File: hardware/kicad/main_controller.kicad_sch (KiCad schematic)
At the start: 39 parts, among them J3 Tag-Connect_TC2050-IDC-NL, SW1 KMR233GLFG, SW2 KMR233GLFG, U6 ESP32-S3-MINI-1, Y1 32.768 kHz

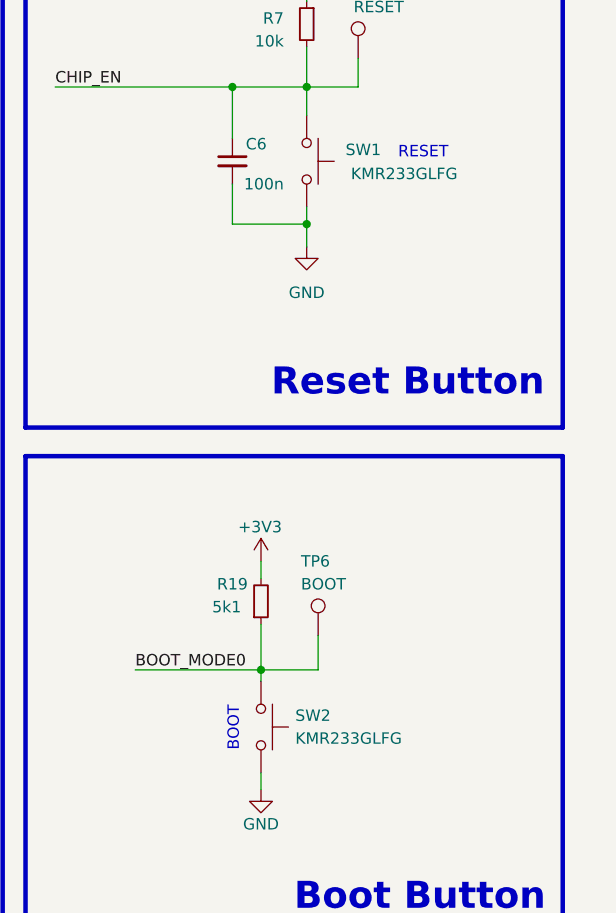
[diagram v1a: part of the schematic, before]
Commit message: fix incorrect bill of material
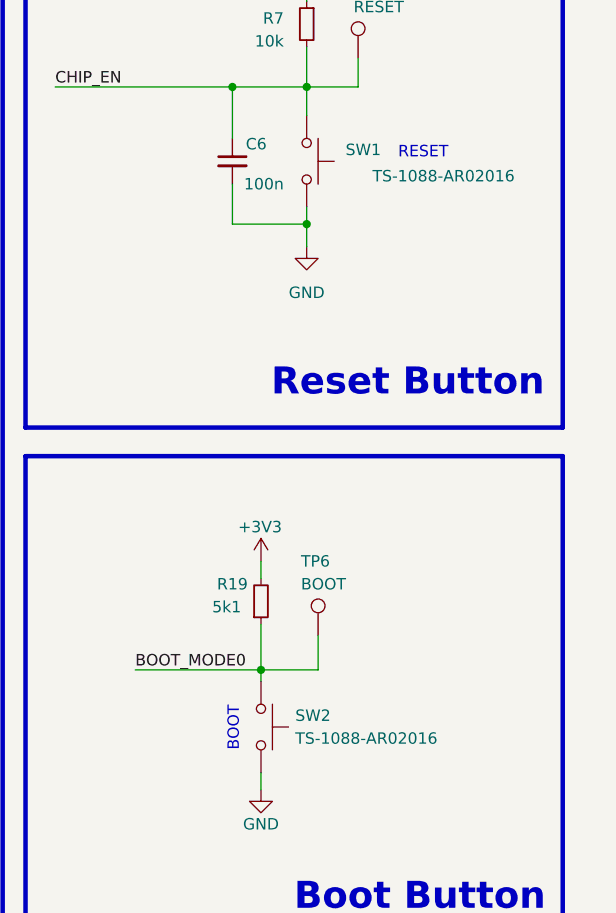
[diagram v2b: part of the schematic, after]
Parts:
- SW1, SW2: value KMR233GLFG -> TS-1088-AR02016; Distributor Link https://www.lcsc.com/product-detail/Tactile-Switches_C-K-KM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 -> https://www.lcsc.com/product-detail/Tactile-Switches_XUNPU-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; Distributor Part Number C2689601 -> C720477; Manufacturer C&K -> XUNPU; Manufacturer Part Number KMR233GLFG -> TS-1088-AR02016
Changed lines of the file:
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@@
 			)
 		)
-		(property "Value" "KMR233GLFG"
+		(property "Value" "TS-1088-AR02016"
 			(at 243.84 114.3 90)
 			(effects
@@
 			)
 		)
-		(property "Datasheet" "https://www.lcsc.com/datasheet/lcsc_datasheet_2203281730_C-K-KMR233GLFG_C2689601.pdf"
+		(property "Datasheet" "https://www.lcsc.com/datasheet/lcsc_datasheet_2304140030_XUNPU-TS-1088-AR02016_C720477.pdf"
 			(at 245.11 113.03 0)
 			(effects
@@
 			)
 		)
-		(property "Description" "Round Button 10mA Brick nogging SPST - NO 300gf 32V SMD Tactile Switches ROHS"
+		(property "Description" "50mA 4mm 100MΩ 100,000 Times 12V 160gf 3mm 2mm Round Button Brick nogging SPST SMD Tactile Switches ROHS"
 			(at 240.03 113.03 0)
 			(effects
@@
 			)
 		)
-		(property "Manufacturer" "C&K"
+		(property "Manufacturer" "XUNPU"
 			(at 240.03 113.03 0)
 			(effects
@@
 			)
 		)
-		(property "Manufacturer Part Number" "KMR233GLFG"
+		(property "Manufacturer Part Number" "TS-1088-AR02016"
 			(at 240.03 113.03 0)
 			(effects
@@
 			)
 		)
-		(property "Distributor Part Number" "C2689601"
+		(property "Distributor Part Number" "C720477"
 			(at 240.03 113.03 0)
 			(effects
@@
 			)
 		)
-		(property "Distributor Link" "https://www.lcsc.com/product-detail/Tactile-Switches_C-K-KMR233GLFG_C2689601.html"
+		(property "Distributor Link" "https://www.lcsc.com/product-detail/Tactile-Switches_XUNPU-TS-1088-AR02016_C720477.html"
 			(at 240.03 113.03 0)
 			(effects
@@
 			)
 		)
-		(property "Value" "KMR233GLFG"
-			(at 261.874 51.562 90)
+		(property "Value" "TS-1088-AR02016"
+			(at 268.224 51.816 90)
 			(effects
 				(font
@@
 			)
 		)
-		(property "Datasheet" "https://www.lcsc.com/datasheet/lcsc_datasheet_2203281730_C-K-KMR233GLFG_C2689601.pdf"
+		(property "Datasheet" "https://www.lcsc.com/datasheet/lcsc_datasheet_2304140030_XUNPU-TS-1088-AR02016_C720477.pdf"
 			(at 250.19 50.165 0)
 			(effects
@@
 			)
 		)
-		(property "Description" "Round Button 10mA Brick nogging SPST - NO 300gf 32V SMD Tactile Switches ROHS"
+		(property "Description" "50mA 4mm 100MΩ 100,000 Times 12V 160gf 3mm 2mm Round Button Brick nogging SPST SMD Tactile Switches ROHS"
 			(at 245.11 50.165 0)
 			(effects
@@
 			)
 		)
-		(property "Manufacturer" "C&K"
+		(property "Manufacturer" "XUNPU"
 			(at 245.11 50.165 0)
 			(effects
@@
 			)
 		)
-		(property "Manufacturer Part Number" "KMR233GLFG"
+		(property "Manufacturer Part Number" "TS-1088-AR02016"
 			(at 245.11 50.165 0)
 			(effects
@@
 			)
 		)
-		(property "Distributor Part Number" "C2689601"
+		(property "Distributor Part Number" "C720477"
 			(at 245.11 50.165 0)
 			(effects
@@
 			)
 		)
-		(property "Distributor Link" "https://www.lcsc.com/product-detail/Tactile-Switches_C-K-KMR233GLFG_C2689601.html"
+		(property "Distributor Link" "https://www.lcsc.com/product-detail/Tactile-Switches_XUNPU-TS-1088-AR02016_C720477.html"
 			(at 245.11 50.165 0)
 			(effects

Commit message: Start Rev 3
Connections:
- net GNSS_EN: no longer U6.9 (GPIO5/TOUCH5/ADC1_CH4)
- net GNSS_FO: no longer U6.8 (GPIO4/TOUCH4/ADC1_CH3)
- net GNSS_RESET: no longer U6.5 (GPIO1/TOUCH1/ADC1_CH0)
- net GNSS_RXD: no longer U6.10 (GPIO6/TOUCH6/ADC1_CH5)
- net GNSS_SDBY: no longer U6.6 (GPIO2/TOUCH2/ADC1_CH1)
- net GNSS_TXD: no longer U6.11 (GPIO7/TOUCH7/ADC1_CH6)
- net GNSS_VBCKP_EN: no longer U6.12 (GPIO8/TOUCH8/ADC1_CH7/SUBSPICS1)
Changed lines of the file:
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@@
-	)
-	(junction
-		(at 191.135 73.025)
-		(diameter 0)
-		(color 0 0 0 0)
 	)
 	(junction
@@
 	)
 	(junction
-		(at 196.85 75.565)
-		(diameter 0)
-		(color 0 0 0 0)
-	)
-	(junction
 		(at 38.735 116.205)
 		(diameter 0)
@@
 	)
 	(junction
-		(at 183.515 67.945)
-		(diameter 0)
-		(color 0 0 0 0)
-	)
-	(junction
 		(at 64.135 169.545)
-		(diameter 0)
-		(color 0 0 0 0)
-	)
-	(junction
-		(at 177.8 65.405)
 		(diameter 0)
 		(color 0 0 0 0)
@@
 	(wire
 		(pts
-			(xy 160.02 75.565) (xy 196.85 75.565)
-		)
-		(stroke
-			(width 0)
-			(type default)
-		)
-	)
-	(wire
-		(pts
 			(xy 161.925 47.625) (xy 161.925 40.64)
 		)
@@
 	(wire
 		(pts
-			(xy 160.02 80.645) (xy 168.275 80.645)
-		)
-		(stroke
-			(width 0)
-			(type default)
-		)
-	)
-	(wire
-		(pts
 			(xy 160.02 111.125) (xy 168.275 111.125)
 		)
@@
 	(wire
 		(pts
-			(xy 160.02 78.105) (xy 168.275 78.105)
-		)
-		(stroke
-			(width 0)
-			(type default)
-		)
-	)
-	(wire
-		(pts
 			(xy 41.91 57.15) (xy 45.085 57.15)
 		)
@@
 	(wire
 		(pts
-			(xy 160.02 83.185) (xy 168.275 83.185)
-		)
-		(stroke
-			(width 0)
-			(type default)
-		)
-	)
-	(wire
-		(pts
-			(xy 160.02 65.405) (xy 177.8 65.405)
-		)
-		(stroke
-			(width 0)
-			(type default)
-		)
-	)
-	(wire
-		(pts
 			(xy 50.165 57.15) (xy 45.085 57.15)
 		)
@@
 	(wire
 		(pts
-			(xy 160.02 67.945) (xy 183.515 67.945)
-		)
-		(stroke
-			(width 0)
-			(type default)
-		)
-	)
-	(wire
-		(pts
 			(xy 160.02 62.865) (xy 175.26 62.865)
 		)
 		(stroke
-			(width 0)
-			(type default)
-		)
-	)
-	(wire
-		(pts
-			(xy 160.02 73.025) (xy 191.135 73.025)
-		)
-		(stroke

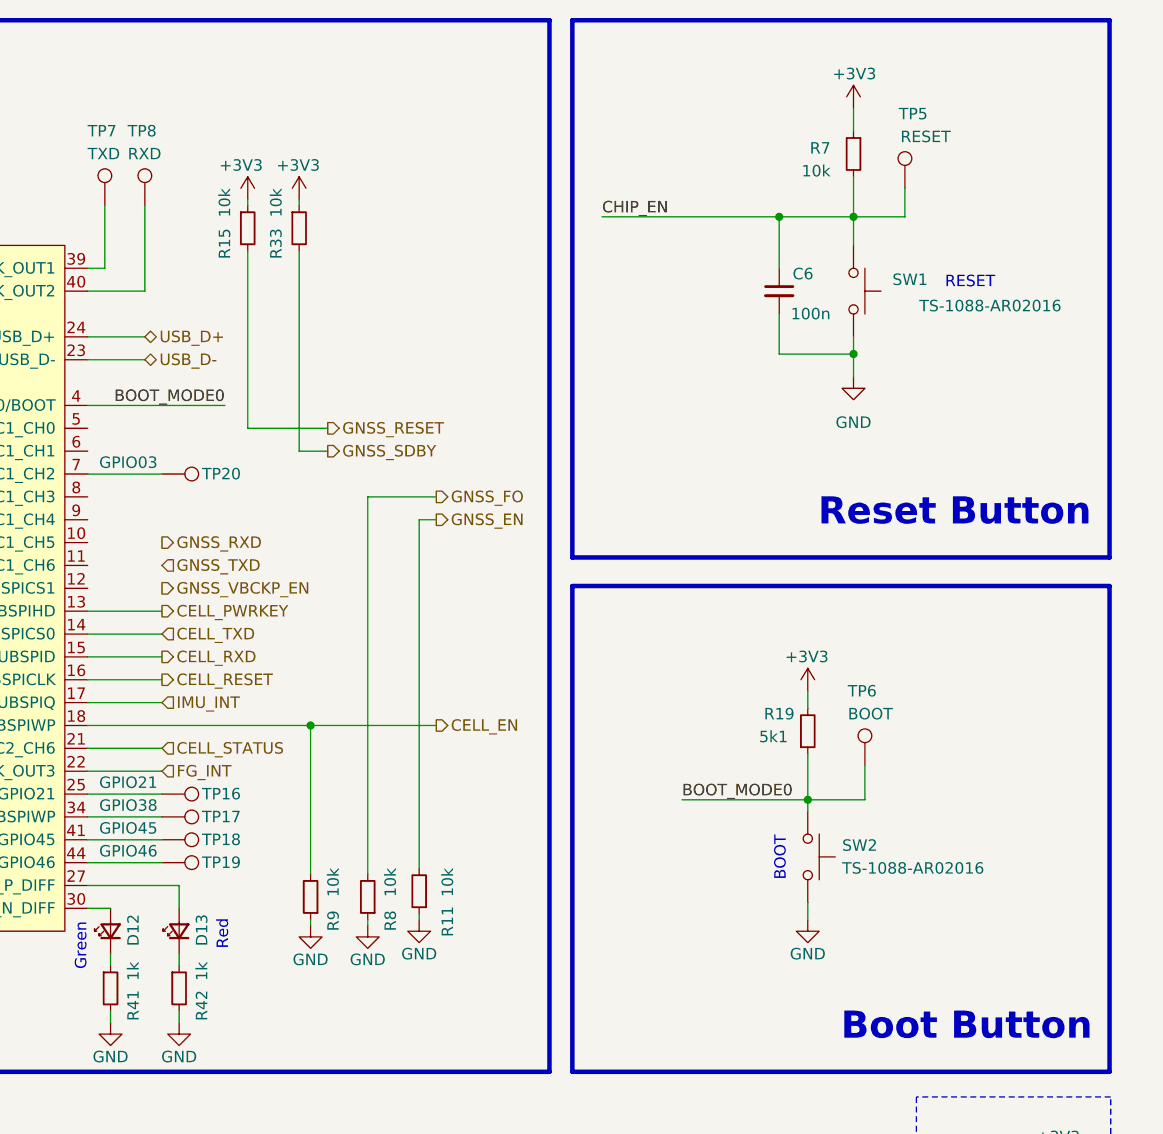
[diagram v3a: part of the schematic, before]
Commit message: GNSS and Antenna Update
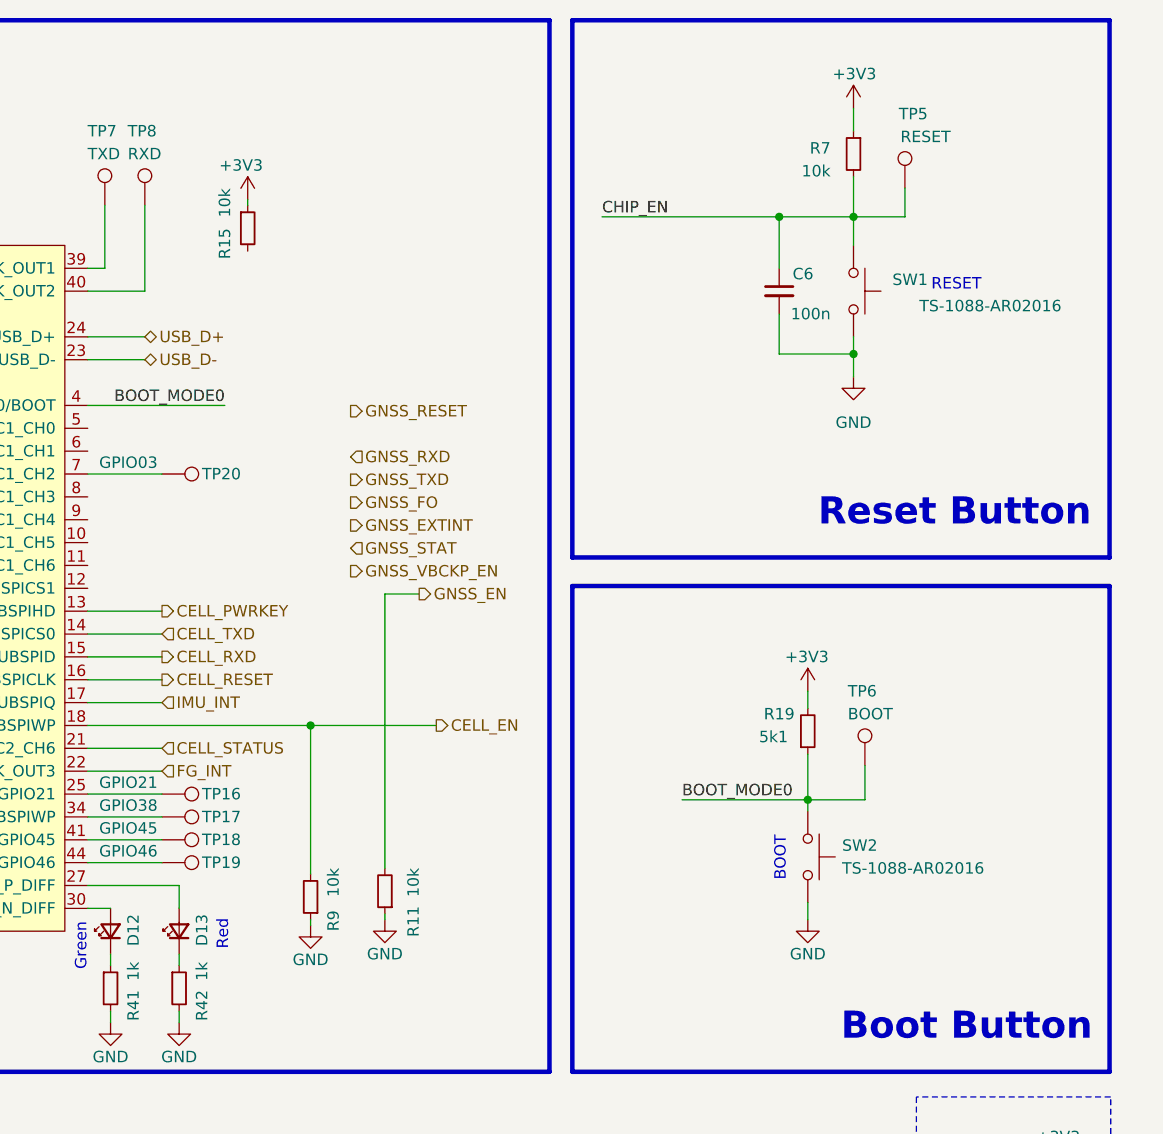
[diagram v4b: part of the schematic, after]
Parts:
- removed R33, R8: 10k, Resistor_SMD:R_0402_1005Metric, symbol Device:R_Small
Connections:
- net GNSS_RESET: no longer R15.2
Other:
- moved on the sheet: R11

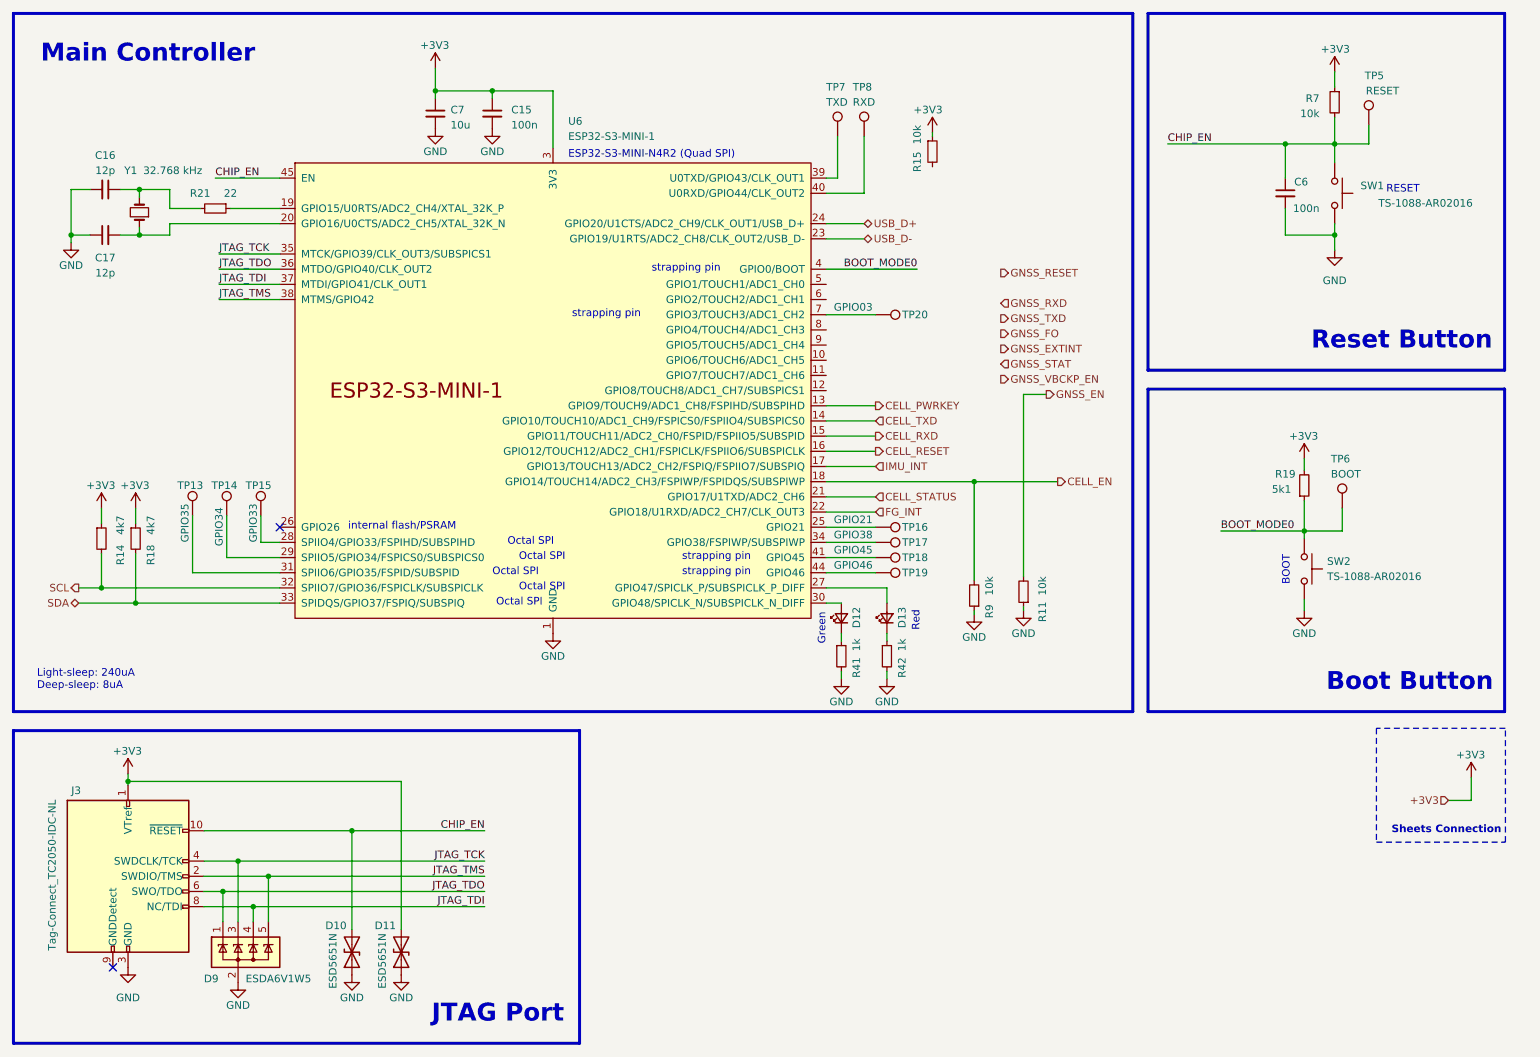
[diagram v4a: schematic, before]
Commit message: Update Sch for GNSS and main controller
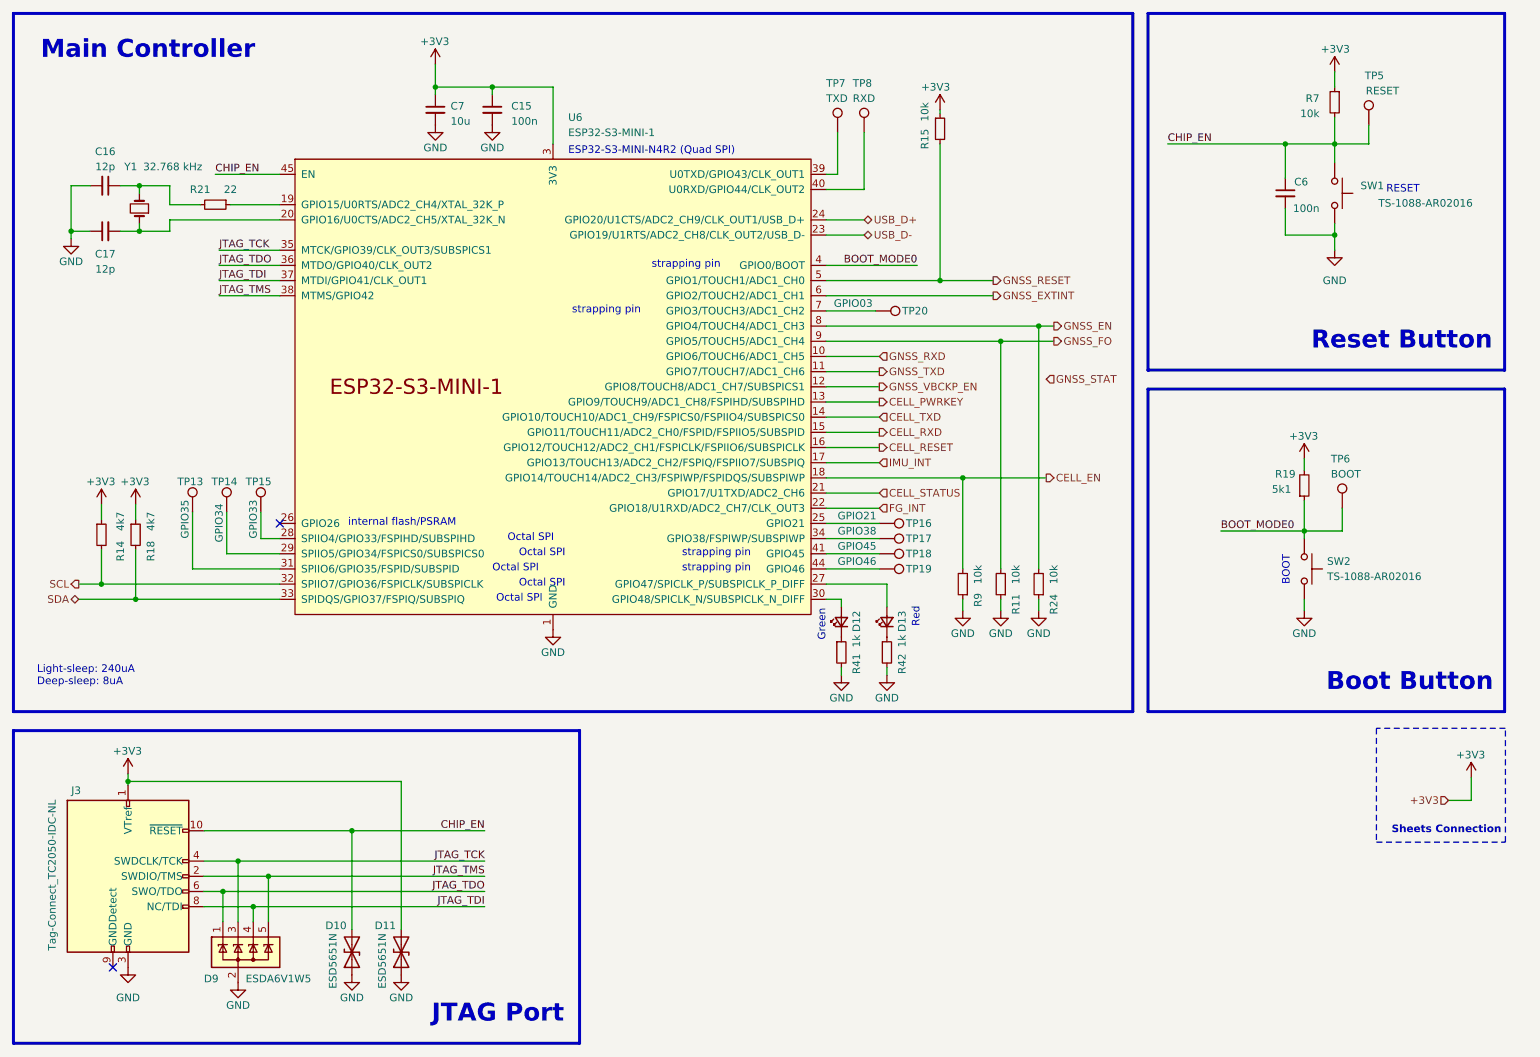
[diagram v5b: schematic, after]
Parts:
- added R24: 10k, Resistor_SMD:R_0402_1005Metric, symbol Device:R_Small
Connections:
- net GND: now also R24.1
- net GNSS_EN: now also U6.8 (GPIO4/TOUCH4/ADC1_CH3), R24.2; no longer R11.2
- net GNSS_EXTINT: now also U6.6 (GPIO2/TOUCH2/ADC1_CH1)
- net GNSS_FO: now also R11.2, U6.9 (GPIO5/TOUCH5/ADC1_CH4)
- net GNSS_RESET: now also R15.2, U6.5 (GPIO1/TOUCH1/ADC1_CH0)
- net GNSS_RXD: now also U6.10 (GPIO6/TOUCH6/ADC1_CH5)
- net GNSS_TXD: now also U6.11 (GPIO7/TOUCH7/ADC1_CH6)
- net GNSS_VBCKP_EN: now also U6.12 (GPIO8/TOUCH8/ADC1_CH7/SUBSPICS1)
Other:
- moved on the sheet: C15, C16, C17, C7, D12, D13, R11, R14, R15, R18, R21, R41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

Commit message: Update for PCB Layout
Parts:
- renumbered C7 to C16, C15 to C17, C16 to C18, C6 to C19, C17 to C20, D12 to D5, D13 to D6, D9 to D7, D10 to D8, D11 to D9, J3 to J2, R7 to R13, R15 to R14, R21 to R15, R19 to R16, R14 to R17, R9 to R19, R11 to R20, R24 to R21, R41 to R22, R42 to R23, TP20 to TP10, TP6 to TP11, TP13 to TP12, TP14 to TP13, TP15 to TP14, TP16 to TP15, TP17 to TP16, TP18 to TP17, TP19 to TP18, TP5 to TP7, TP7 to TP8, TP8 to TP9, U6 to U3
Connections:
- net GNSS_EN: now also R20.2, U3.9 (GPIO5/TOUCH5/ADC1_CH4); no longer R21.2, U3.8 (GPIO4/TOUCH4/ADC1_CH3)
- net GNSS_FO: now also R21.2, U3.8 (GPIO4/TOUCH4/ADC1_CH3); no longer R20.2, U3.9 (GPIO5/TOUCH5/ADC1_CH4)

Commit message: Finish Manufacturing File
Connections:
- net CELL_EN: now also U3.17 (GPIO13/TOUCH13/ADC2_CH2/FSPIQ/FSPIIO7/SUBSPIQ); no longer U3.18 (GPIO14/TOUCH14/ADC2_CH3/FSPIWP/FSPIDQS/SUBSPIWP)
- net GNSS_EN: now also R21.2, U3.8 (GPIO4/TOUCH4/ADC1_CH3); no longer R20.2, U3.9 (GPIO5/TOUCH5/ADC1_CH4)
- net GNSS_EXTINT: now also U3.10 (GPIO6/TOUCH6/ADC1_CH5); no longer U3.6 (GPIO2/TOUCH2/ADC1_CH1)
- net GNSS_FO: now also R20.2, U3.9 (GPIO5/TOUCH5/ADC1_CH4); no longer R21.2, U3.8 (GPIO4/TOUCH4/ADC1_CH3)
- net GNSS_RXD: now also U3.11 (GPIO7/TOUCH7/ADC1_CH6); no longer U3.10 (GPIO6/TOUCH6/ADC1_CH5)
- net GNSS_STAT: now also TP15.1, U3.25 (GPIO21)
- net GNSS_TXD: now also U3.12 (GPIO8/TOUCH8/ADC1_CH7/SUBSPICS1); no longer U3.11 (GPIO7/TOUCH7/ADC1_CH6)
- net GNSS_VBCKP_EN: now also U3.6 (GPIO2/TOUCH2/ADC1_CH1); no longer U3.12 (GPIO8/TOUCH8/ADC1_CH7/SUBSPICS1)
- net IMU_INT: now also U3.18 (GPIO14/TOUCH14/ADC2_CH3/FSPIWP/FSPIDQS/SUBSPIWP); no longer U3.17 (GPIO13/TOUCH13/ADC2_CH2/FSPIQ/FSPIIO7/SUBSPIQ)

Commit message: update
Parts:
- added TP24, TP25, TP28: ~, TestPoint:TestPoint_Pad_D1.0mm, symbol Connector:TestPoint
- TP15: value GPIO21 -> ~
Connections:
- net GNSS_FO: now also TP24.1
- net GNSS_RESET: now also TP25.1
- net GNSS_STAT: now also TP28.1
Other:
- note added: "Test Pad"
- moved on the sheet: TP15
